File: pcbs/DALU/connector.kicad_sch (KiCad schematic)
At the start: 4 parts, among them J201 Conn_02x20_Odd_Even, U201 74HC245, U202 74HC245, U203 74HC245

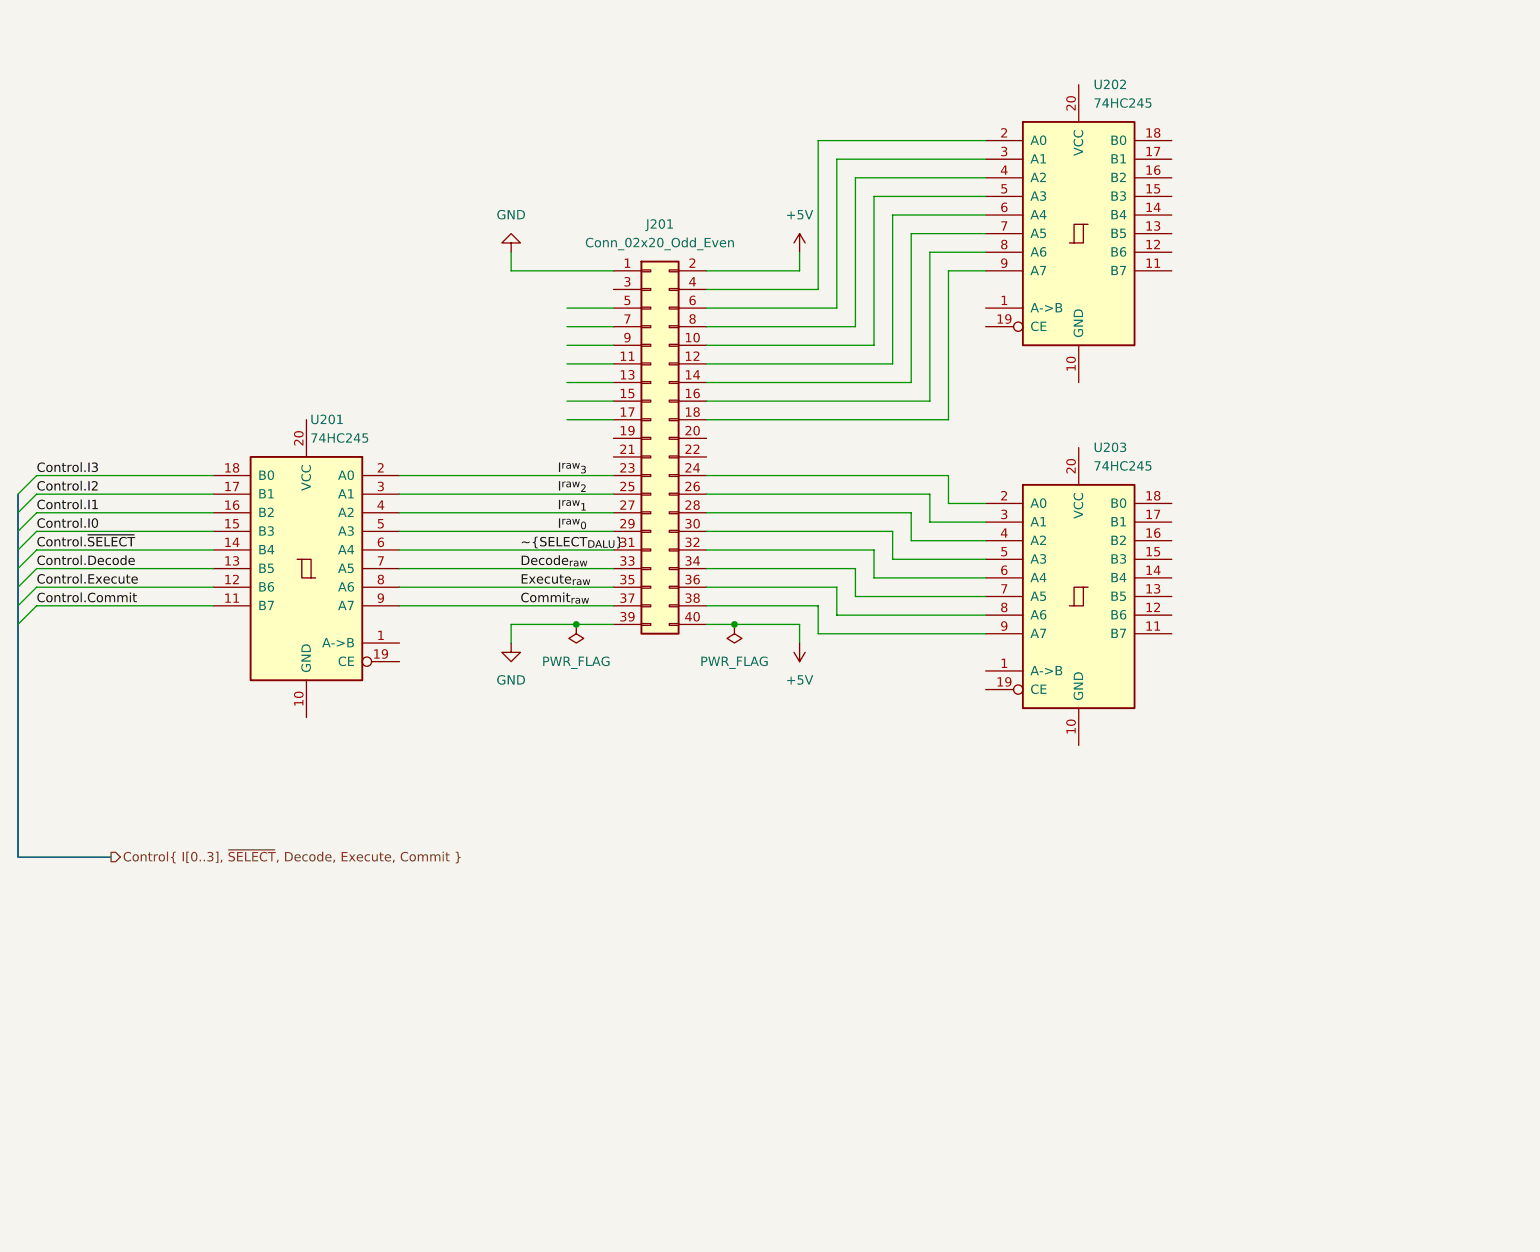
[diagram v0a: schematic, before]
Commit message: Input stage fiddling
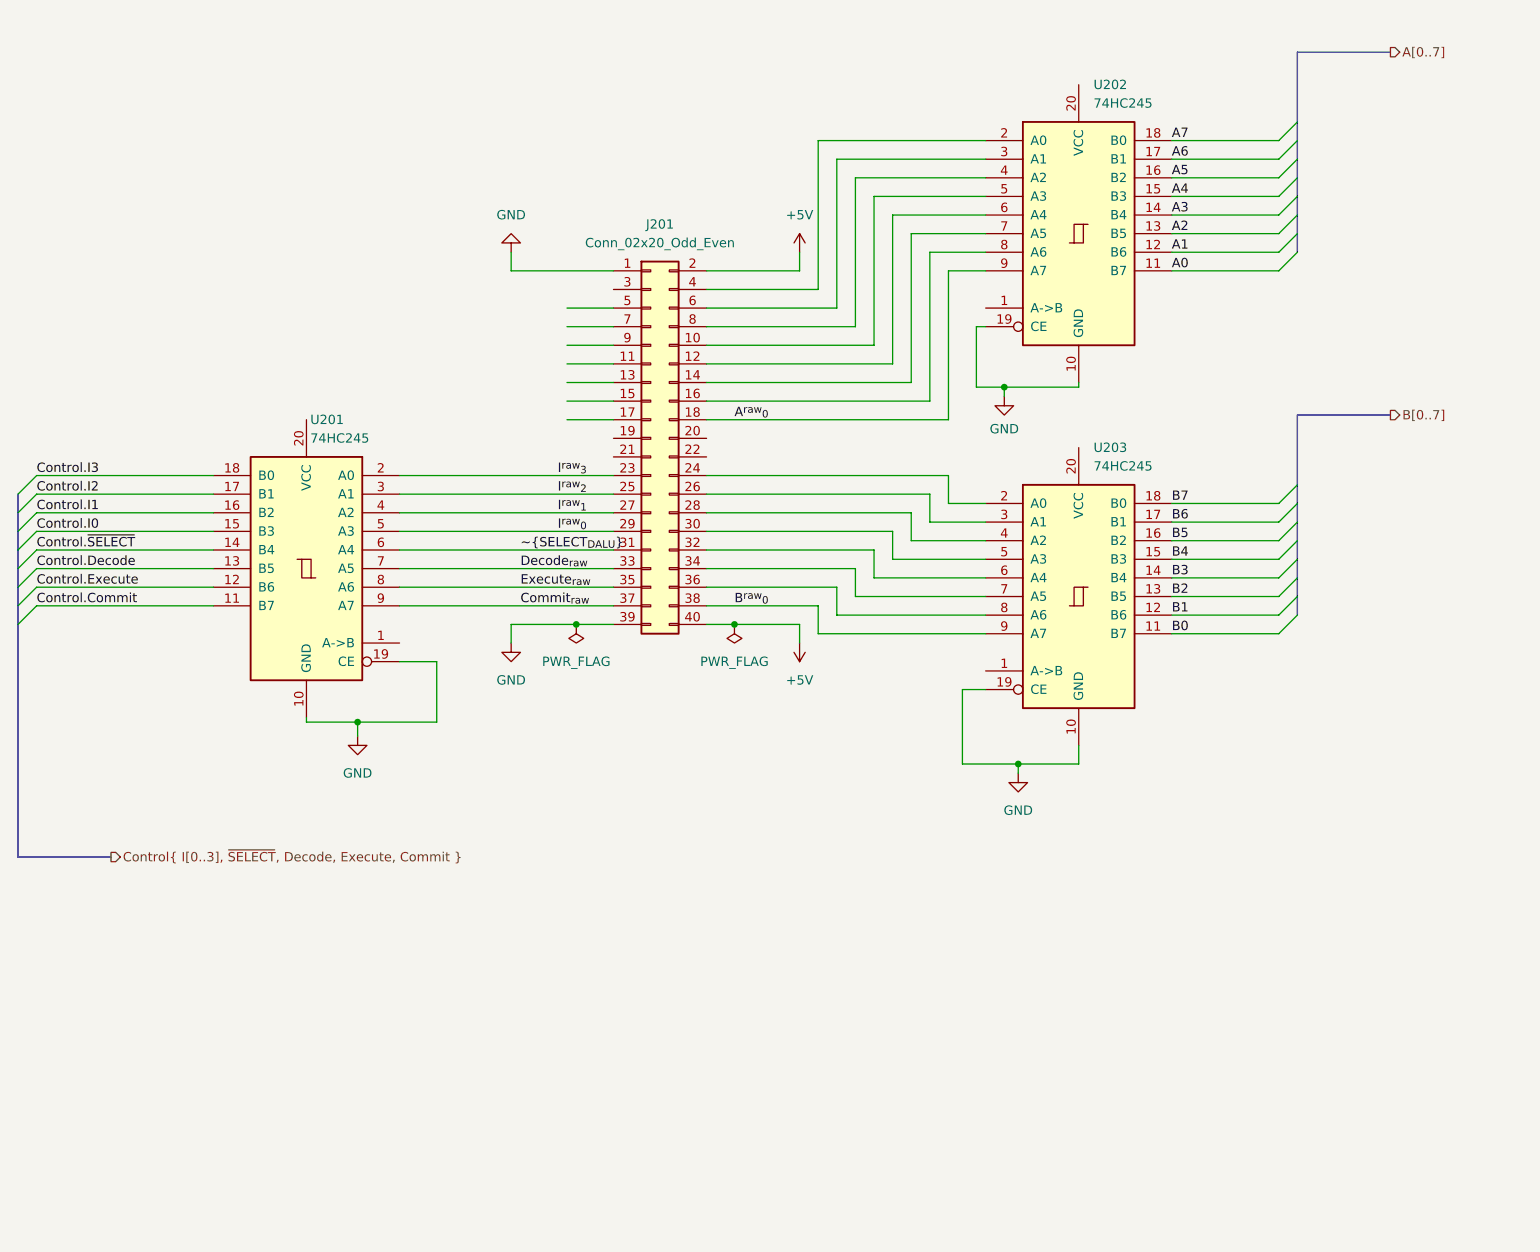
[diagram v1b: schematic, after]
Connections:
- net GND: now also U201.10 (GND), U201.19 (CE), U202.10 (GND), U202.19 (CE), U203.10 (GND), U203.19 (CE)
- net B0: now reaches U203.11 (B7)
- net B1: now reaches U203.12 (B6)
- net B2: now reaches U203.13 (B5)
- net B3: now reaches U203.14 (B4)
- net B4: now reaches U203.15 (B3)
- net B5: now reaches U203.16 (B2)
- net B6: now reaches U203.17 (B1)
- net B7: now reaches U203.18 (B0)
- net B^{raw}_{0}: now reaches J201.38 (Pin_38), U203.9 (A7)
- net A^{raw}_{0}: now reaches J201.18 (Pin_18), U202.9 (A7)
- net A0: now reaches U202.11 (B7)
- net A1: now reaches U202.12 (B6)
- net A2: now reaches U202.13 (B5)
- net A3: now reaches U202.14 (B4)
- net A4: now reaches U202.15 (B3)
- net A5: now reaches U202.16 (B2)
- net A6: now reaches U202.17 (B1)
- net A7: now reaches U202.18 (B0)

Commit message: Starting to think about decoding etc.
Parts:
- added RN201, RN202: 10k, Resistor_SMD:R_Array_Convex_4x0402, symbol Device:R_Pack04
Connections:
- net +5V: now also RN202.8 (R1.2)
- net Control.Commit: now also RN202.4 (R4.1)
- net Control.Decode: now also RN202.2 (R2.1)
- net Control.Execute: now also RN202.3 (R3.1)
- net Control.I0: now also RN201.4 (R4.1)
- net Control.I1: now also RN201.3 (R3.1)
- net Control.I2: now also RN201.2 (R2.1)
- net Control.I3: now also RN201.1 (R1.1)
- net Control.~{SELECT}: now also RN202.1 (R1.1)
- net GND: now also RN201.5 (R4.2), RN201.6 (R3.2), RN201.7 (R2.2), RN201.8 (R1.2), RN202.5 (R4.2), RN202.6 (R3.2), RN202.7 (R2.2); no longer U201.19 (CE)
- net ~{SELECT_{DALU}}: now also U201.19 (CE)

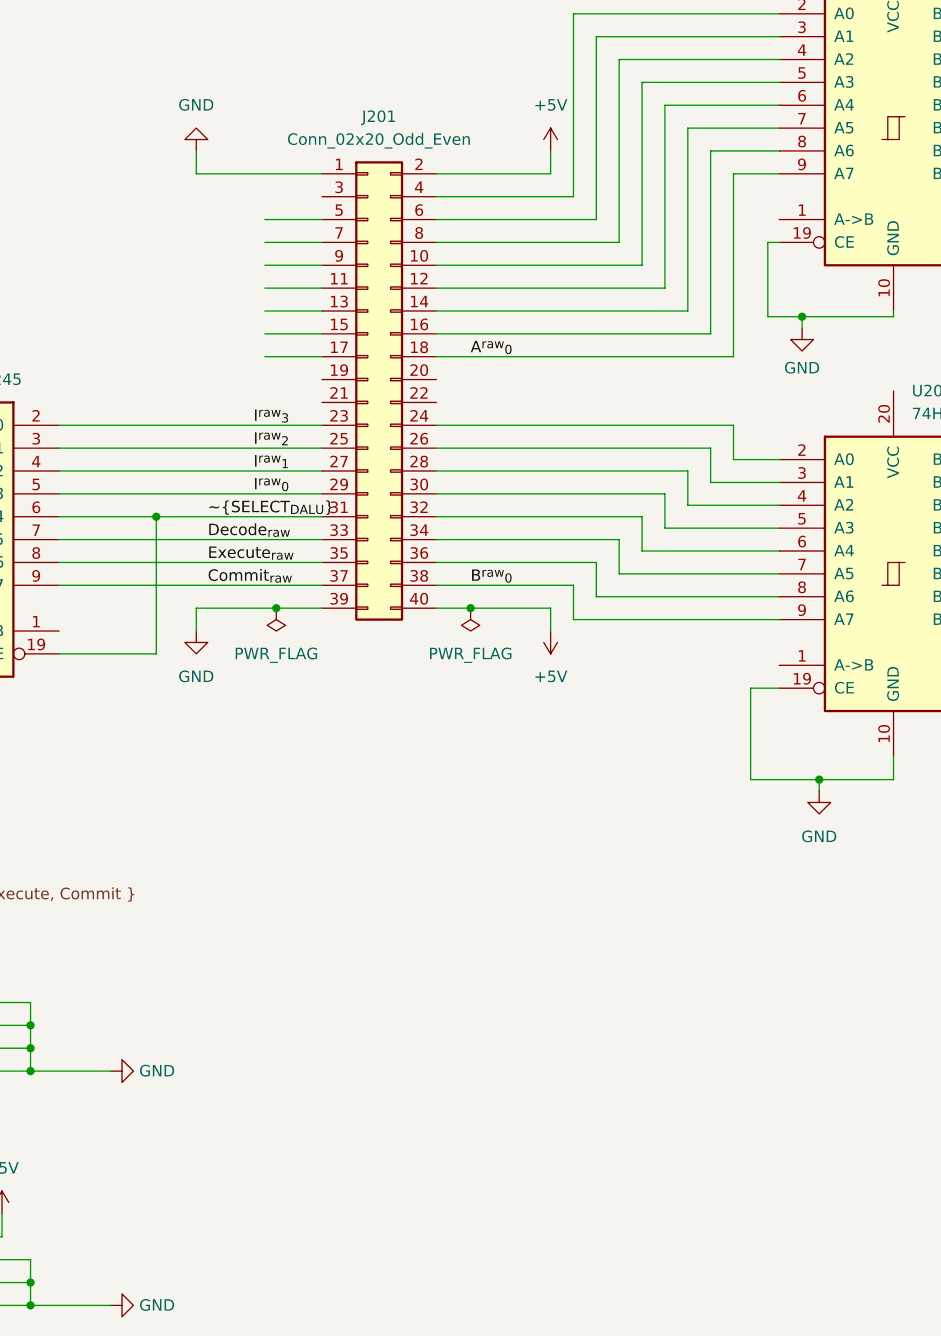
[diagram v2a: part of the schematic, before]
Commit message: Starting to do the routing. Schematic not yet complete, though
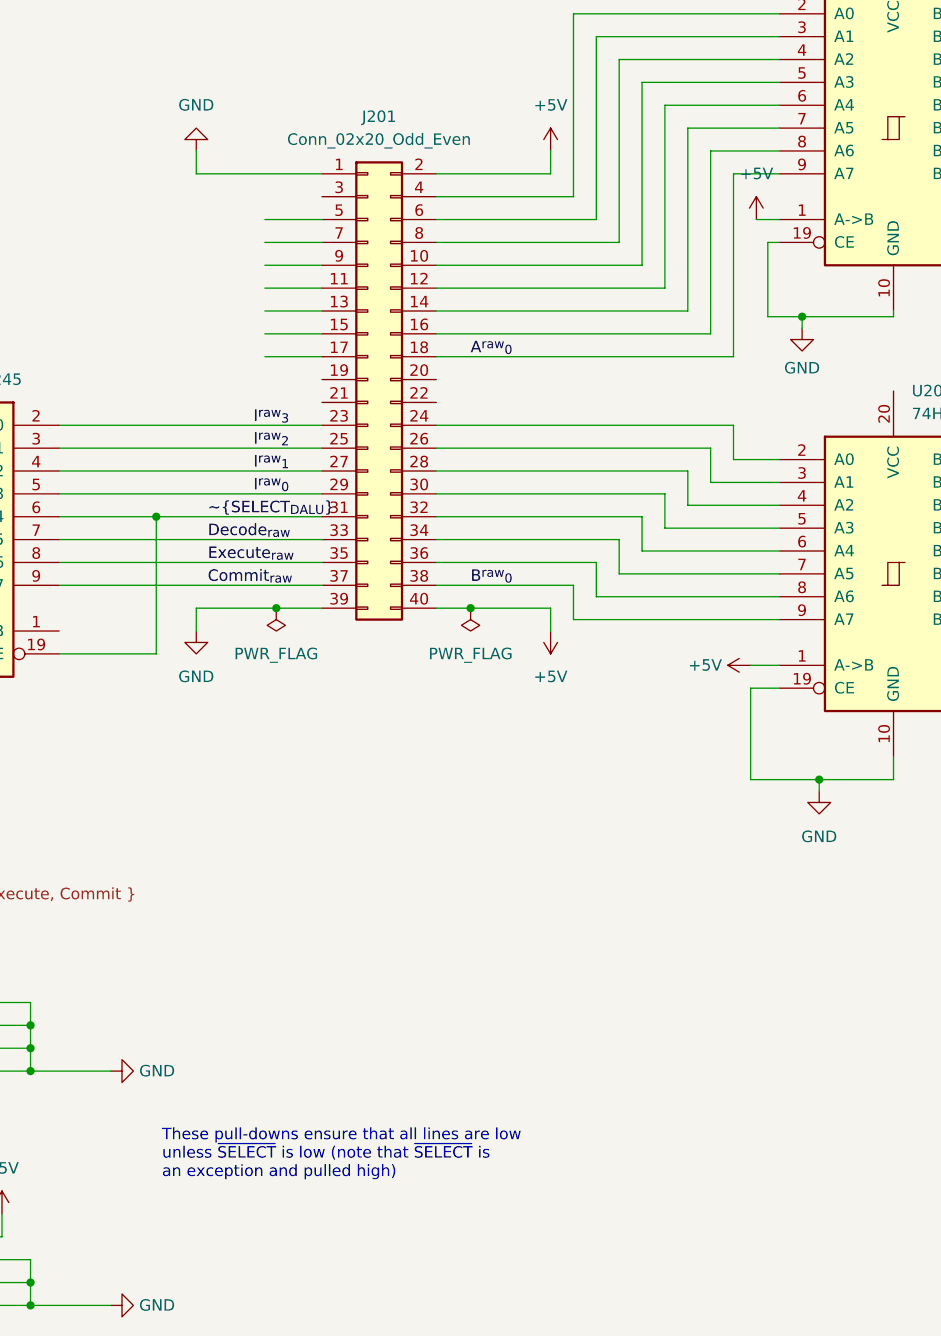
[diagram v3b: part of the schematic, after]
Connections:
- net +5V: now also U202.1 (A->B), U203.1 (A->B)
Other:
- note added: "These pull-downs ensure that all lines are low unless ~{SELECT} is low (note that ~{SELECT} is an exception and pulled high)"
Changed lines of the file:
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@@
+    (stroke (width 0) (type default) (color 0 0 0 0))
+  )
+  (wire (pts (xy 148.59 69.85) (xy 151.13 69.85))
     (stroke (width 0) (type default) (color 0 0 0 0))
   )
@@
     (stroke (width 0) (type default) (color 0 0 0 0))
   )
+  (wire (pts (xy 147.955 119.38) (xy 151.13 119.38))
+    (stroke (width 0) (type default) (color 0 0 0 0))
+  )
   (wire (pts (xy 176.53 62.23) (xy 191.135 62.23))
     (stroke (width 0) (type default) (color 0 0 0 0))
@@
   (wire (pts (xy 113.03 64.77) (xy 125.73 64.77))
     (stroke (width 0) (type default) (color 0 0 0 0))
+  )
+  (text "These pull-downs ensure that all lines are low\nunless ~{SELECT} is low (note that ~{SELECT} is\nan exception and pulled high)"
+    (at 82.55 176.53 0)
+    (effects (font (size 1.27 1.27)) (justify left bottom))
   )
   (label "Control.I1" (at 21.59 161.925 0)
@@
   (symbol (lib_id "power:GND") (at 153.67 81.915 0) (unit 1)
     (in_bom yes) (on_board yes) (fields_autoplaced)
-    (property "Reference" "#PWR0209" (id 0) (at 153.67 88.265 0)
+    (property "Reference" "#PWR0211" (id 0) (at 153.67 88.265 0)
       (effects (font (size 1.27 1.27)) hide)
     )
@@
     (pin "8")
     (pin "9")
+  )
+  (symbol (lib_id "power:+5V") (at 148.59 69.85 0) (unit 1)
+    (in_bom yes) (on_board yes) (fields_autoplaced)
+    (property "Reference" "#PWR0210" (id 0) (at 148.59 73.66 0)
+      (effects (font (size 1.27 1.27)) hide)
+    )
+    (property "Value" "+5V" (id 1) (at 148.59 64.77 0))
+    (property "Footprint" "" (id 2) (at 148.59 69.85 0)
+      (effects (font (size 1.27 1.27)) hide)
+    )
+    (property "Datasheet" "" (id 3) (at 148.59 69.85 0)
+      (effects (font (size 1.27 1.27)) hide)
+    )
+    (pin "1")
   )
   (symbol (lib_id "power:GND") (at 76.835 164.465 90) (unit 1)
@@
   (symbol (lib_id "power:GND") (at 155.575 133.35 0) (unit 1)
     (in_bom yes) (on_board yes) (fields_autoplaced)
-    (property "Reference" "#PWR0210" (id 0) (at 155.575 139.7 0)
+    (property "Reference" "#PWR0212" (id 0) (at 155.575 139.7 0)
       (effects (font (size 1.27 1.27)) hide)
     )
@@
     (pin "8")
   )
+  (symbol (lib_id "power:+5V") (at 147.955 119.38 90) (unit 1)
+    (in_bom yes) (on_board yes) (fields_autoplaced)
+    (property "Reference" "#PWR0209" (id 0) (at 151.765 119.38 0)
+      (effects (font (size 1.27 1.27)) hide)
+    )
+    (property "Value" "+5V" (id 1) (at 144.78 119.3799 90)
+      (effects (font (size 1.27 1.27)) (justify left))
+    )
+    (property "Footprint" "" (id 2) (at 147.955 119.38 0)
+      (effects (font (size 1.27 1.27)) hide)
+    )
+    (property "Datasheet" "" (id 3) (at 147.955 119.38 0)
+      (effects (font (size 1.27 1.27)) hide)
+    )
+    (pin "1")
+  )
   (symbol (lib_id "Device:R_Pack04") (at 57.15 161.925 270) (unit 1)
